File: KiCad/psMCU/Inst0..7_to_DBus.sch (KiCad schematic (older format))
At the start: 6 parts

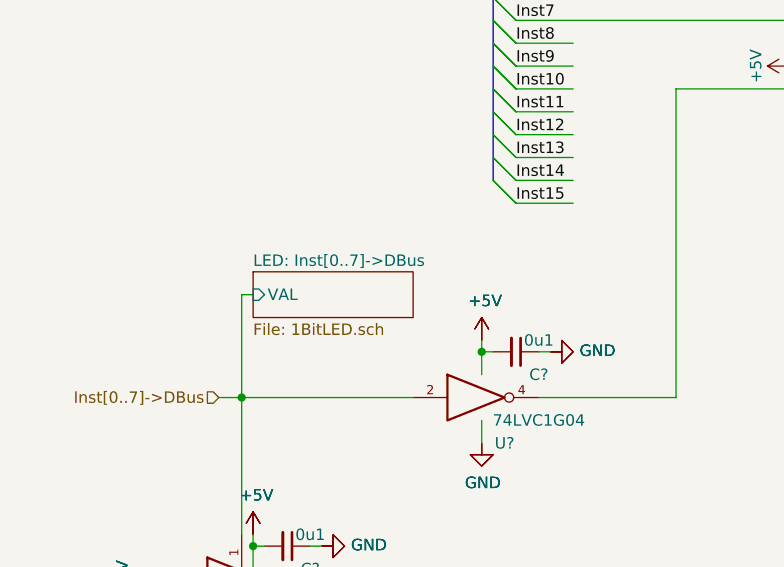
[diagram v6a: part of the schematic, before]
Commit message: Removed Single LED sheets
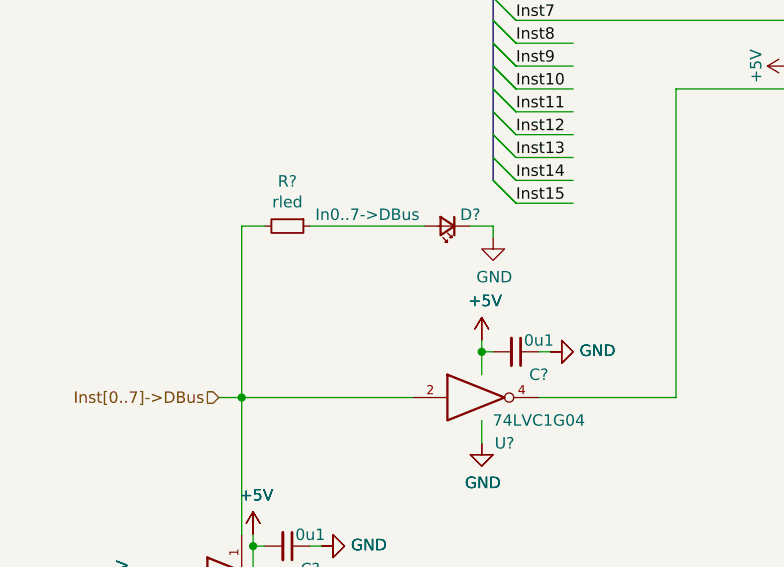
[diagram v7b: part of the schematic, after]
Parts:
- added D?: In0..7->DBus, Diode_SMD:D_0603_1608Metric, symbol Device:LED_Small
- added R?: rled, Resistor_SMD:R_0603_1608Metric, symbol Device:R_Small
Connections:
- wire segments 50 -> 53

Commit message: First Schematic Draft done.
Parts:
- C1, C2, C3: renamed from C?; footprint Capacitor_SMD:C_0603_1608Metric -> NoRef_Footprints:C_0603_1608Metric_NoRef
- D1: renamed from D?; footprint Diode_SMD:D_0603_1608Metric -> NoRef_Footprints:D_0603_1608Metric_NoRef
- R1: renamed from R?; footprint Resistor_SMD:R_0603_1608Metric -> NoRef_Footprints:R_0603_1608Metric
- gave numbers to parts that had none: 3
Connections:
- net labels removed: Inst10, Inst11, Inst12, Inst13, Inst14, Inst15, Inst8, Inst9
- wire segments 53 -> 45
